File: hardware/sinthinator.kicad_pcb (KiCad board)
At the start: 2 copper layers, 100.9 x 116.5 mm, 45 parts, among them J1 3.5mm TRRS, J2 USB-C, M2 MountingHole_2.2mm_M2, SW1 SW_Push, SW2 SW_Push, SW3 SW_Push, U1 CAP1206, U3 MCP4725, U4 CAP1206, U5 CAP1206, U7 AMS1117-3.3, U8 PAM8302A, U9 STM32C011F6

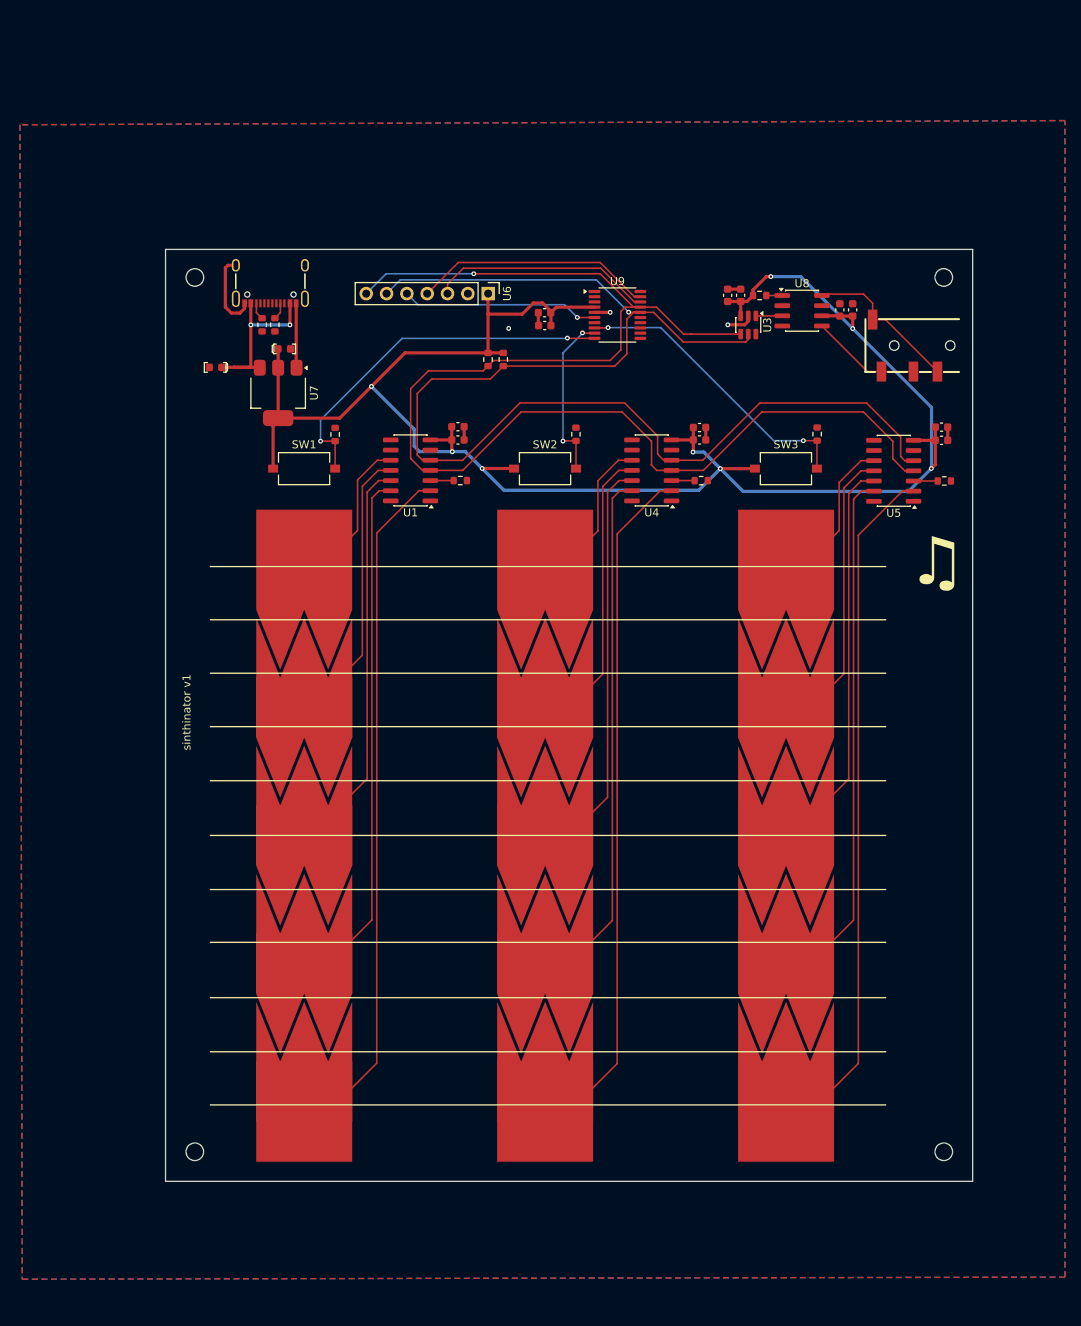
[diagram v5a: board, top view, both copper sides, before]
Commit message: Update touch slider dimensions + route i2c mux
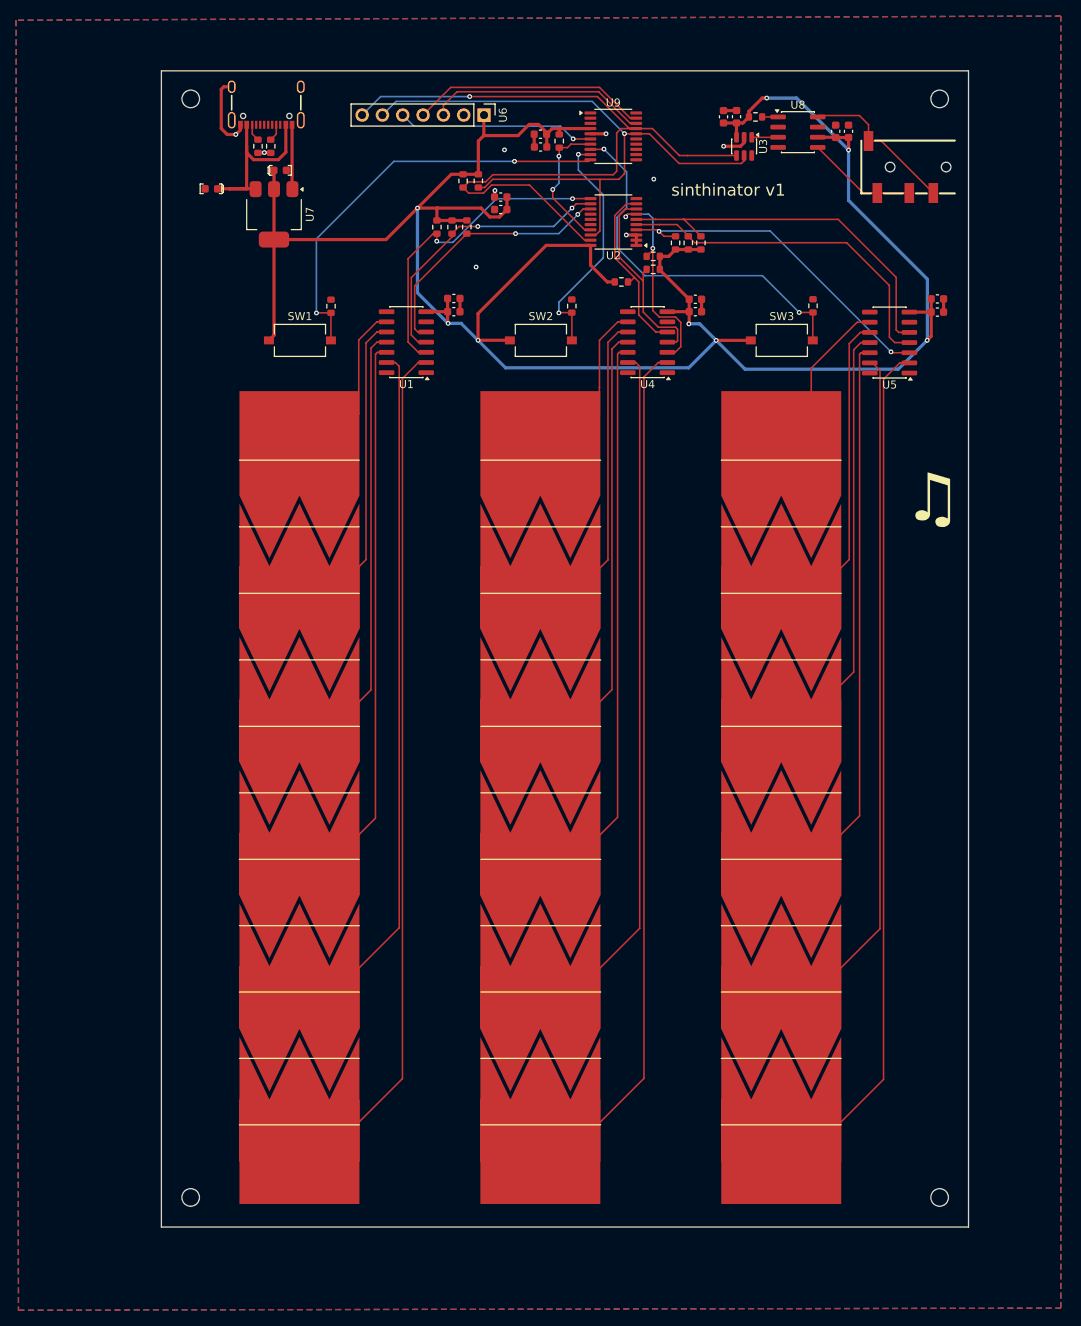
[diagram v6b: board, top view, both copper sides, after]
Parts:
- added C15: 1uF, PCM_SparkFun-Capacitor:C_0603_1608Metric, F.Cu at (142.0, 36.9)
- added C16: 0.1uF, PCM_SparkFun-Capacitor:C_0603_1608Metric, F.Cu at (142.0, 35.3)
- added R12: 2.2k, PCM_SparkFun-Resistor:R_0603_1608Metric, F.Cu at (165.4, 41.0)
- added R13: 2.2k, PCM_SparkFun-Resistor:R_0603_1608Metric, F.Cu at (167.0, 41.0)
- added R14: 2.2k, PCM_SparkFun-Resistor:R_0603_1608Metric, F.Cu at (163.9, 41.0)
- added R15: 2.2k, PCM_SparkFun-Resistor:R_0603_1608Metric, F.Cu at (161.1, 42.7)
- added R16: 2.2k, PCM_SparkFun-Resistor:R_0603_1608Metric, F.Cu at (161.1, 44.3)
- added R17: 2.2k, PCM_SparkFun-Resistor:R_0603_1608Metric, F.Cu at (157.1, 45.9)
- added R18: 2.2k, PCM_SparkFun-Resistor:R_0603_1608Metric, F.Cu at (149.3, 28.3)
- added U2: PCA9544APW, Package_SO:TSSOP-20_4.4x6.5mm_P0.65mm, F.Cu at (156.1, 38.4)
- R3, R4, R5: value 10k -> 1k
- R6: value 10k -> 4.7k
- R7, R8, R9: value 1k -> 2.2k
- UTouch1, UTouch2, UTouch3: footprint Slider:TouchSlider-5_80x12mm -> Slider:TouchSlider-6_100x15mm
- moved R9 69.2 mm to (135.9, 39.1), turned to -90 degrees
- moved R8 43.2 mm to (137.8, 39.0), turned to -90 degrees
- moved R7 31.8 mm to (134.0, 39.1), turned to -90 degrees
- moved R1 22.5 mm to (139.2, 33.3)
- moved R2 22.5 mm to (137.3, 33.3)
- moved J1 22.3 mm to (194.2, 31.5)
- moved J2 22.3 mm to (112.7, 26.6)
- moved R10 22.3 mm to (113.3, 28.9)
- moved R11 22.3 mm to (111.7, 28.9)
- moved C3 22.3 mm to (105.8, 34.3)
- moved C4 22.3 mm to (114.4, 32.0)
- moved C5 22.3 mm to (183.9, 27.1)
- moved C6 22.3 mm to (185.5, 27.1)
- moved C7 22.3 mm to (169.8, 25.3)
- moved C8 22.3 mm to (171.5, 25.3)
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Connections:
- R7 pad 1: Net-(U1-ALERT#) -> 3.3V
- R7 pad 2: GND -> Net-(U1-ALERT#)
- R8 pad 1: Net-(U4-ALERT#) -> 3.3V
- R8 pad 2: GND -> Net-(U1-SMCLK)
- R9 pad 1: Net-(U5-ALERT#) -> 3.3V
- R9 pad 2: GND -> Net-(U1-SMDATA)
- U1 pad 4: I2C_SDA -> Net-(U1-SMDATA)
- U1 pad 5: I2C_SCK -> Net-(U1-SMCLK)
- U1 pad 9: GND -> Net-(U1-CS6)
- U4 pad 3: Net-(U4-ALERT#) -> Net-(U2-~{INT1})
- U4 pad 4: I2C_SDA -> Net-(U2-SD1)
- U4 pad 5: I2C_SCK -> Net-(U2-SC1)
- U4 pad 9: GND -> Net-(U4-CS6)
- U5 pad 3: Net-(U5-ALERT#) -> Net-(U2-~{INT0})
- U5 pad 4: I2C_SDA -> Net-(U2-SD0)
- U5 pad 5: I2C_SCK -> Net-(U2-SC0)
- U5 pad 9: GND -> Net-(U5-CS6)
- U9 pad 7: unconnected-(U9-PA0-Pad7) -> I2C_INT
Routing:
- net I2C_SCK: track 169.8 -> 82.6 mm
- net I2C_SDA: track 174.1 -> 97.8 mm
- net 3.3V: track 234.2 -> 306.0 mm
- net Net-(U2-SC0): track 0.00 -> 46.9 mm
- net Net-(U2-SD0): track 0.00 -> 44.1 mm
- net Net-(U2-~{INT0}): track 0.00 -> 42.8 mm, vias 0 -> 2
- net Net-(U1-ALERT#): track 2.92 -> 40.6 mm, vias 0 -> 2
- net Net-(U1-SMDATA): track 0.00 -> 35.9 mm, vias 0 -> 2
- net Net-(U1-SMCLK): track 0.00 -> 33.0 mm, vias 0 -> 2
- net Net-(U5-CS6): track 0.00 -> 29.5 mm
- net Net-(U4-CS6): track 0.00 -> 29.3 mm
- net Net-(U1-CS6): track 0.00 -> 29.3 mm
- net Net-(U2-~{INT1}): track 0.00 -> 27.3 mm, vias 0 -> 2
- net Net-(U2-SD1): track 0.00 -> 25.4 mm
- net Net-(U1-CS3): track 44.1 -> 67.6 mm
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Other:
- board size 100.9 x 116.5 mm -> 100.9 x 144.5 mm

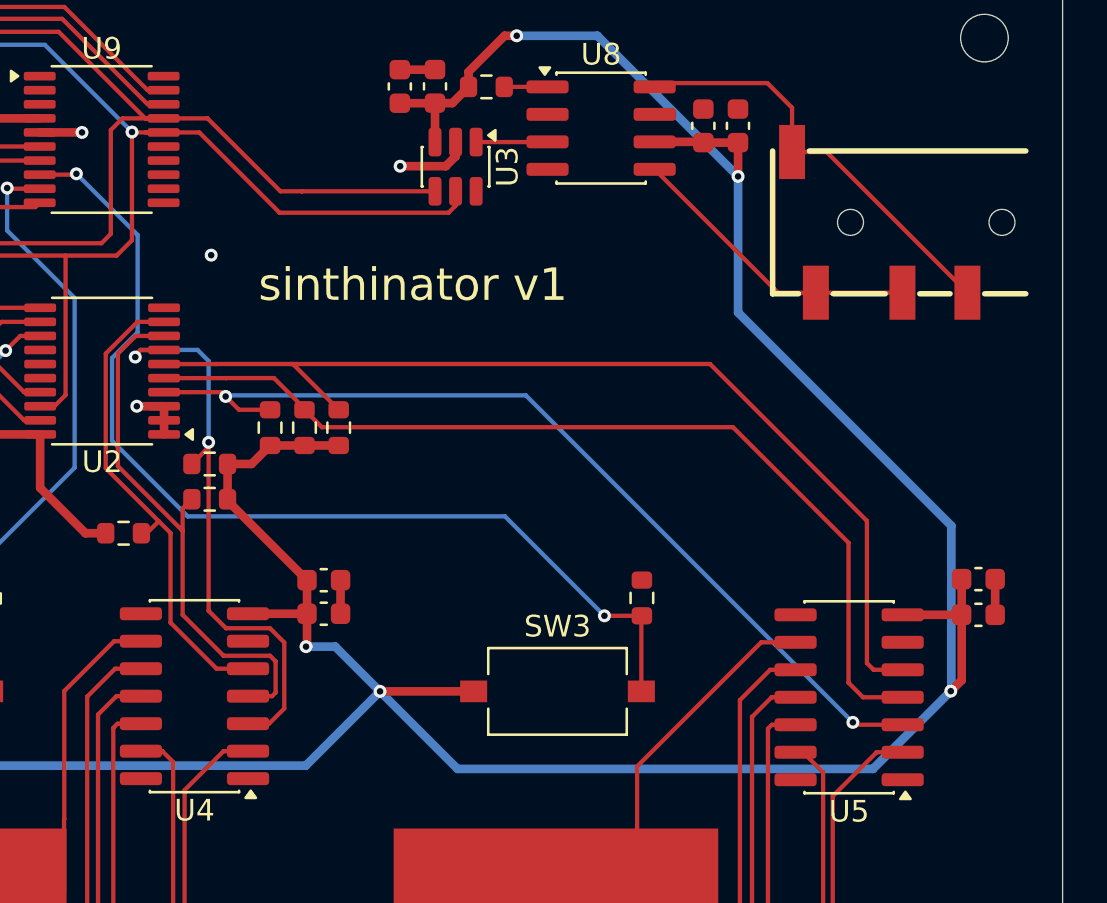
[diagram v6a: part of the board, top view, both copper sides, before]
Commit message: Add potentiometer for the audio output
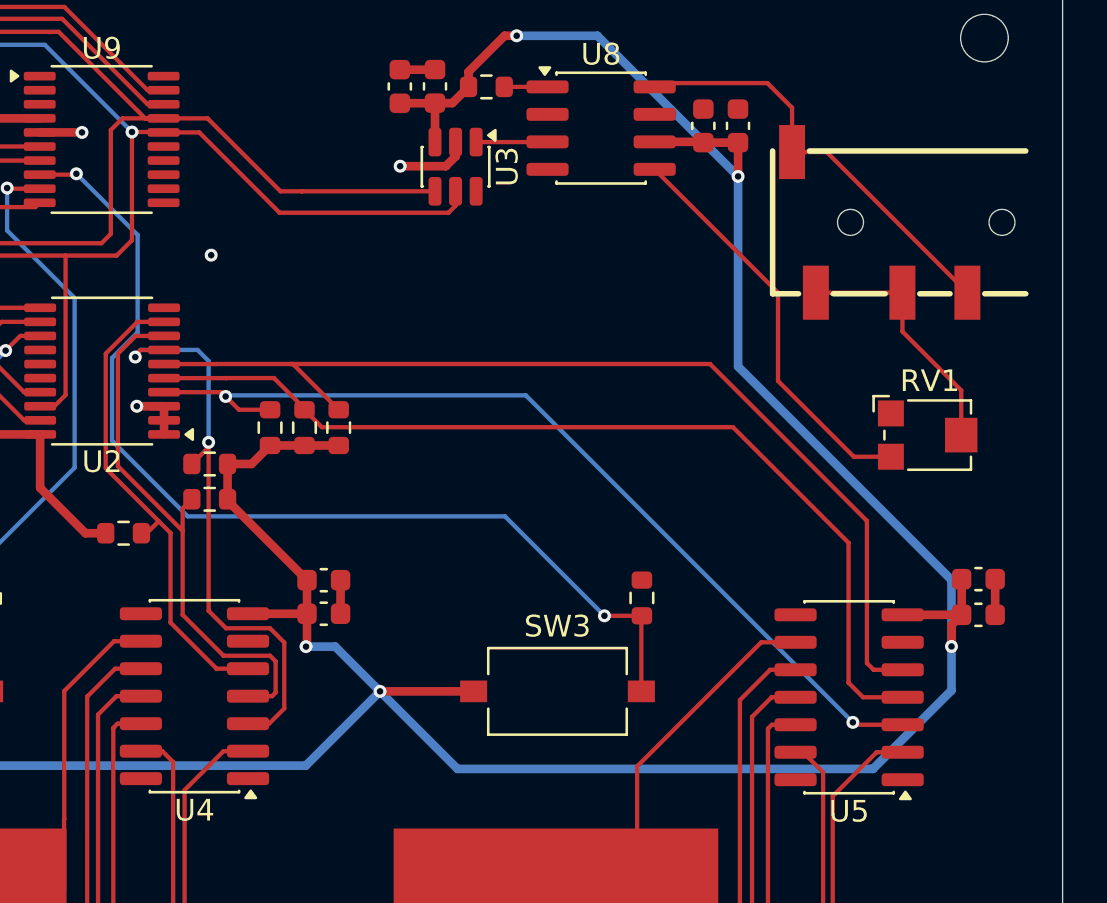
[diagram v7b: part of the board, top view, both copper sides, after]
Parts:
- added RV1: R_Potentiometer, Potentiometer_SMD:Potentiometer_Bourns_TC33X_Vertical, F.Cu at (194.3, 41.4)
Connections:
- J1 pad R1: Net-(U8-OUT+) -> Net-(J1-PadR1)
- J1 pad T: Net-(U8-OUT+) -> Net-(J1-PadR1)
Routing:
- net Net-(J1-PadR1): track 0.00 -> 11.7 mm
- net Net-(U8-OUT+): track 13.8 -> 18.8 mm
- net 3.3V: track 306.0 -> 304.0 mm
- net I2C_SCK: track 82.6 -> 81.8 mm
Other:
- board text added: "feat. mc badback, lil' tonedef and weird al ways"

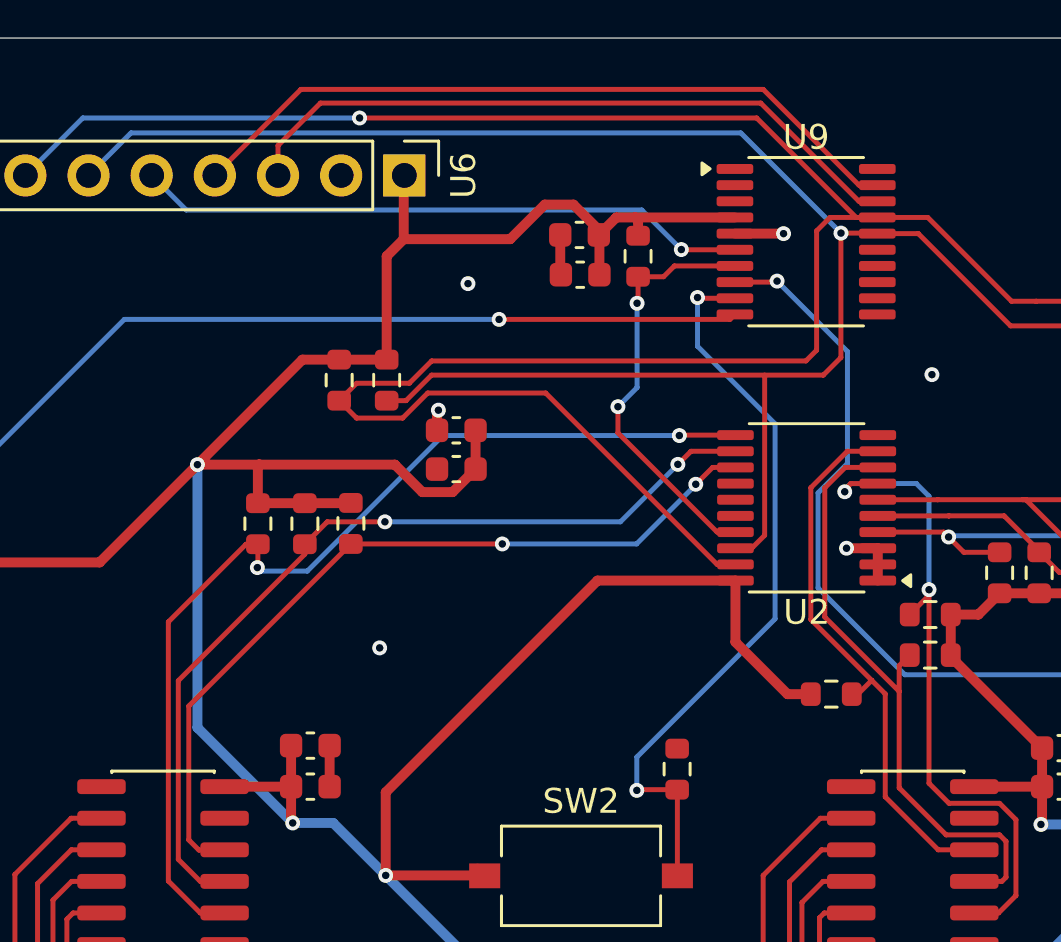
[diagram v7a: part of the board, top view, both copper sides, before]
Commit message: Fix caps position + move some vias
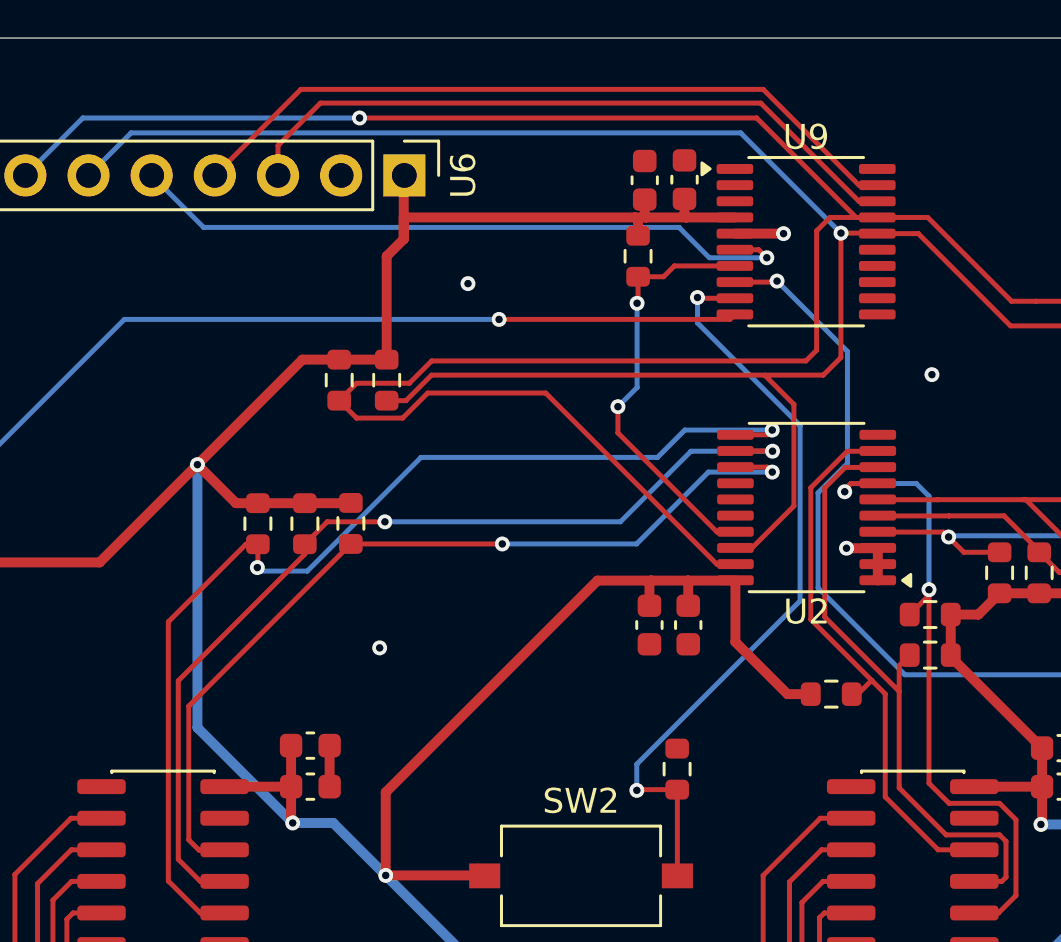
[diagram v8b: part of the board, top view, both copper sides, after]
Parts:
- R1, R12, R13, R14, R18, R2, R7, R8, R9: value 2.2k -> 4.7k
- moved C15 11.2 mm to (151.3, 43.1), turned to -90 degrees
- moved C16 11.0 mm to (149.8, 43.1), turned to -90 degrees
- moved C2 4.77 mm to (151.2, 25.2), turned to 90 degrees
- moved C1 4.60 mm to (149.6, 25.2), turned to 90 degrees
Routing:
- net 3.3V: track 304.0 -> 293.2 mm
- net Net-(U1-ALERT#): track 40.6 -> 43.7 mm
- net Net-(U1-SMDATA): track 35.9 -> 38.9 mm
- net Net-(U1-SMCLK): track 33.0 -> 35.9 mm
- net NRST: track 24.7 -> 27.5 mm
- net GND: track 36.8 -> 34.4 mm, vias 9 -> 8
- net I2C_SCK: track 81.8 -> 82.8 mm
- net Net-(U9-PA2): track 30.0 -> 30.9 mm
